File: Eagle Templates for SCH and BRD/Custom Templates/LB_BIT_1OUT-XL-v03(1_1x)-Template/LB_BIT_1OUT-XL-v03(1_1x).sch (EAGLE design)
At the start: 7 parts, among them U6 LV321SOT23-5

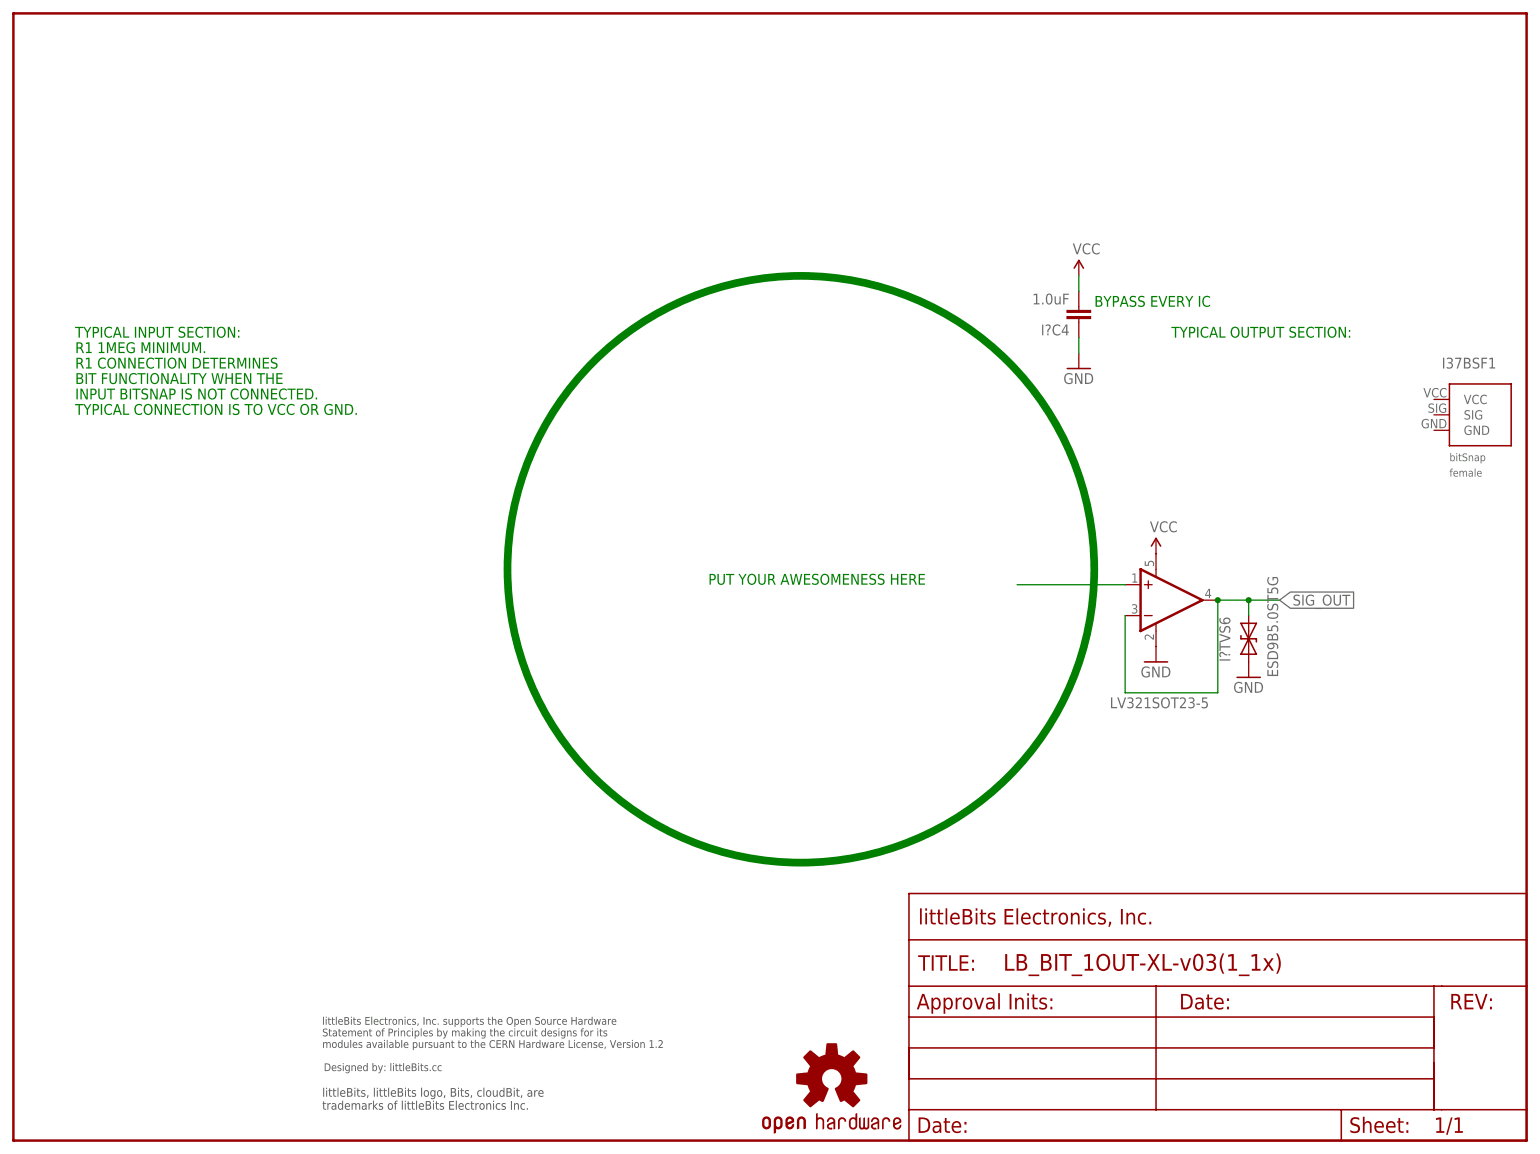
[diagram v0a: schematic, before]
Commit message: Updated templates
- Added ferrite beads
- Moved text and annotations off of Nets layer
- Minor layout changes
- Removed I/O/W prefix from reference designators
- Removed output stage components from output bits
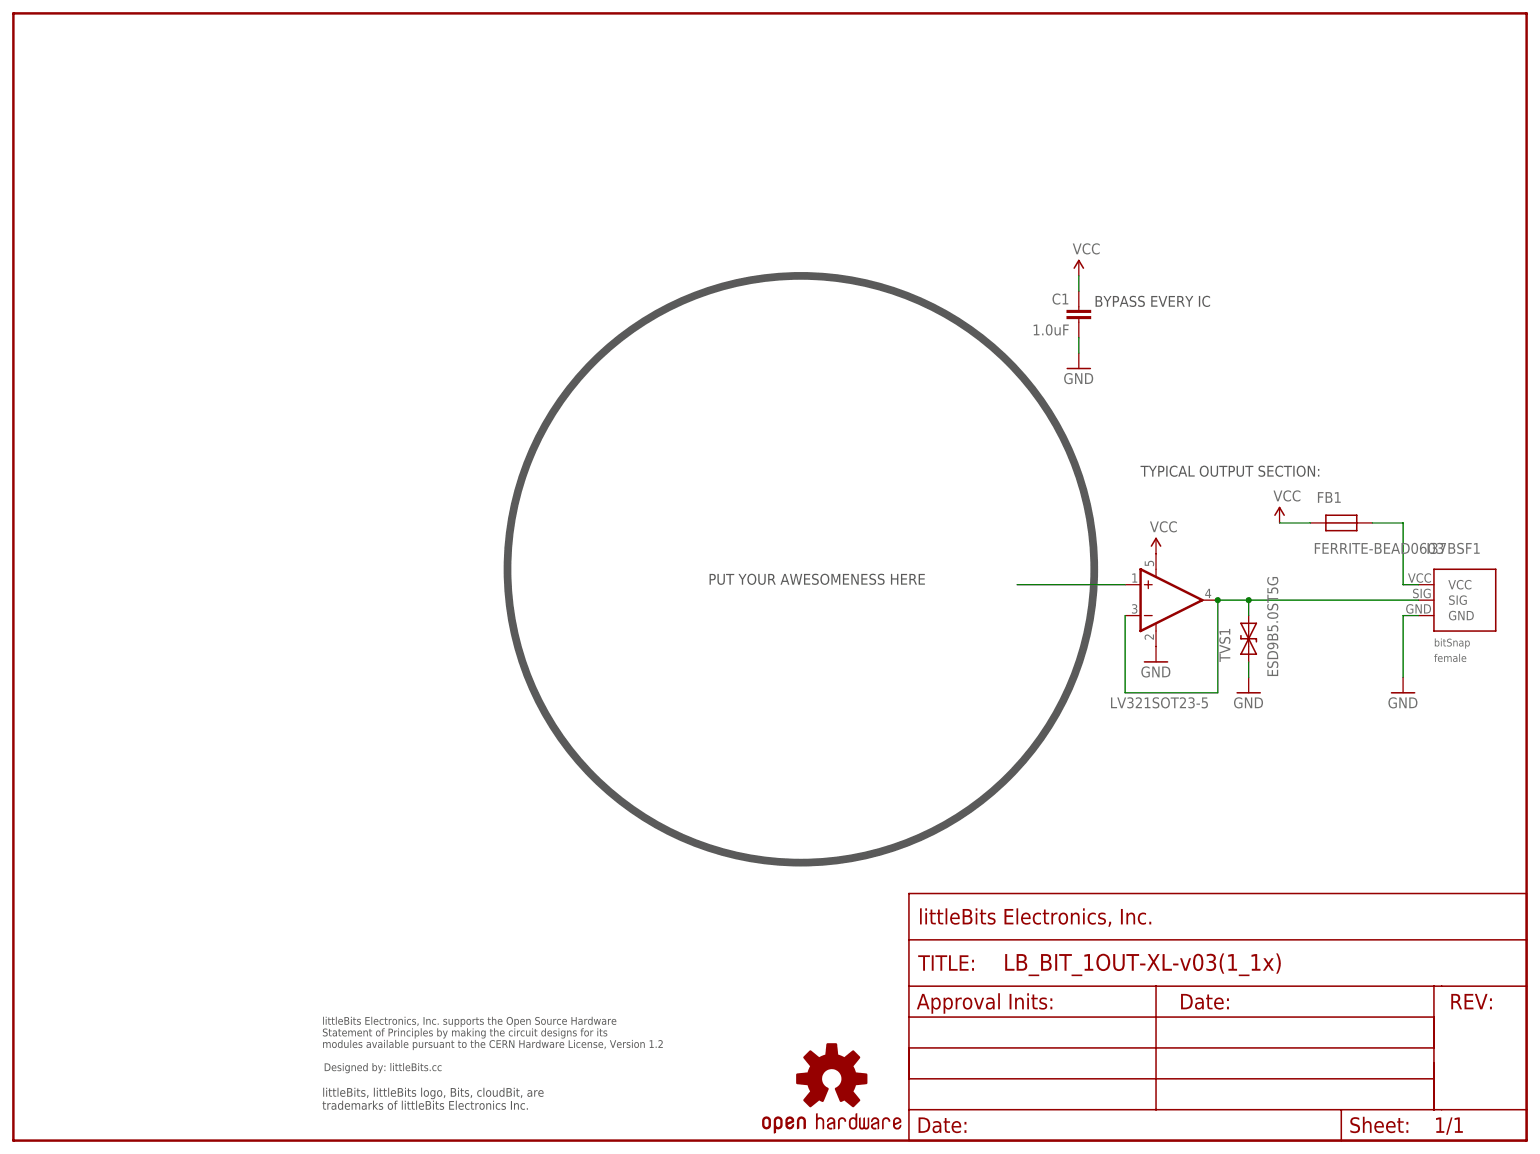
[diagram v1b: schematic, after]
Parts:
- added FB1: FERRITE-BEAD0603, LITTLEBITS:FERRITE-BEAD0603
- FRAME1: value FRAME-LETTER -> FRAME-LETTERWHITEMASK; device LITTLEBITS:FRAME-LETTER -> LITTLEBITS:FRAME-LETTERWHITEMASK
- renumbered I?C4 to C1, I?TVS6 to TVS1, U6 to U1
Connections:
- new net N$1: FB1.P$1, I37BSF1.VCC
- net GND: now also I37BSF1.GND
- net SIG_OUT: now also I37BSF1.SIG
- net VCC: now also FB1.P$2
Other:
- note removed: "BIT FUNCTIONALITY WHEN THE"
- note removed: "INPUT BITSNAP IS NOT CONNECTED."
- note removed: "R1 1MEG MINIMUM."
- note removed: "R1 CONNECTION DETERMINES"
- note removed: "TYPICAL CONNECTION IS TO VCC OR GND."
- note removed: "TYPICAL INPUT SECTION:"
- moved on the sheet: I37BSF1
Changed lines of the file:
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@@
 <?xml version="1.0" encoding="utf-8"?>
 <!DOCTYPE eagle SYSTEM "eagle.dtd">
-<eagle version="6.6.0">
+<eagle version="6.5.0">
 <drawing>
 <settings>
@@
 <layer number="56" name="wert" color="7" fill="1" visible="no" active="no"/>
 <layer number="57" name="tCAD" color="7" fill="1" visible="no" active="no"/>
+<layer number="90" name="Modules" color="5" fill="1" visible="no" active="yes"/>
 <layer number="91" name="Nets" color="2" fill="1" visible="yes" active="yes"/>
 <layer number="92" name="Busses" color="1" fill="1" visible="yes" active="yes"/>
@@
 <layer number="97" name="Info" color="7" fill="1" visible="yes" active="yes"/>
 <layer number="98" name="Guide" color="6" fill="1" visible="no" active="yes"/>
+<layer number="99" name="SpiceOrder" color="7" fill="1" visible="no" active="no"/>
 <layer number="100" name="Muster" color="7" fill="1" visible="no" active="no"/>
 <layer number="101" name="Patch_Top" color="12" fill="4" visible="no" active="yes"/>
@@
 <layer number="251" name="SMDround" color="12" fill="11" visible="no" active="no"/>
 <layer number="254" name="cooling" color="7" fill="1" visible="no" active="yes"/>
+<layer number="255" name="routoute" color="7" fill="1" visible="no" active="yes"/>
 </layers>
 <schematic>
@@
 <part name="I37BSF1" library="bitSnap" deviceset="BITSNAP_V03_FEMALE" device=""/>
 <part name="U$3" library="SparkFun" deviceset="OSHW-LOGO" device="L"/>
-<part name="I?C4" library="LITTLEBITS" deviceset="CAP" device="CAP-0603" value="1.0uF">
+<part name="C1" library="LITTLEBITS" deviceset="CAP" device="CAP-0603" value="1.0uF">
 <attribute name="COMPOSITION" value=""/>
 <attribute name="LB_PN" value=""/>
@@
 <part name="GND17" library="SparkFun" deviceset="GND" device=""/>
 <part name="P+2" library="SparkFun" deviceset="VCC" device=""/>
-<part name="U6" library="LITTLEBITS" deviceset="LV321" device="SOT23-5"/>
+<part name="U1" library="LITTLEBITS" deviceset="LV321" device="SOT23-5"/>
 <part name="GND18" library="SparkFun" deviceset="GND" device=""/>
 <part name="P+3" library="SparkFun" deviceset="VCC" device=""/>
 <part name="GND19" library="SparkFun" deviceset="GND" device=""/>
-<part name="I?TVS6" library="LITTLEBITS" deviceset="DIODE-TVS" device="SOD-923" value="ESD9B5.0ST5G"/>
+<part name="TVS1" library="LITTLEBITS" deviceset="DIODE-TVS" device="SOD-923" value="ESD9B5.0ST5G"/>
 <part name="U$1" library="LITTLEBITS" deviceset="OSHWCREDIT" device=""/>
-<part name="FRAME1" library="LITTLEBITS" deviceset="FRAME-LETTER" device=""/>
+<part name="FRAME1" library="LITTLEBITS" deviceset="FRAME-LETTER" device="WHITEMASK"/>
+<part name="FB1" library="LITTLEBITS" deviceset="FERRITE-BEAD" device="0603"/>
+<part name="P+1" library="SparkFun" deviceset="VCC" device=""/>
+<part name="GND1" library="SparkFun" deviceset="GND" device=""/>
 </parts>
 <sheets>
 <sheet>
 <plain>
-<text x="10.16" y="129.54" size="1.778" layer="91">R1 1MEG MINIMUM.</text>
-<text x="10.16" y="127" size="1.778" layer="91">R1 CONNECTION DETERMINES</text>
-<text x="10.16" y="124.46" size="1.778" layer="91">BIT FUNCTIONALITY WHEN THE</text>
-<text x="10.16" y="121.92" size="1.778" layer="91">INPUT BITSNAP IS NOT CONNECTED.</text>
-<text x="10.16" y="119.38" size="1.778" layer="91">TYPICAL CONNECTION IS TO VCC OR GND.</text>
-<text x="10.16" y="132.08" size="1.778" layer="91">TYPICAL INPUT SECTION:</text>
-<circle x="129.54" y="93.98" radius="48.26" width="1.27" layer="91"/>
-<text x="114.3" y="91.44" size="1.778" layer="91">PUT YOUR AWESOMENESS HERE</text>
-<text x="190.5" y="132.08" size="1.778" layer="91">TYPICAL OUTPUT SECTION:</text>
-<text x="177.8" y="137.16" size="1.778" layer="91">BYPASS EVERY IC</text>
+<circle x="129.54" y="93.98" radius="48.26" width="1.27" layer="97"/>
+<text x="114.3" y="91.44" size="1.778" layer="97">PUT YOUR AWESOMENESS HERE</text>
+<text x="185.42" y="109.22" size="1.778" layer="97">TYPICAL OUTPUT SECTION:</text>
+<text x="177.8" y="137.16" size="1.778" layer="97">BYPASS EVERY IC</text>
 </plain>
 <instances>
-<instance part="I37BSF1" gate="G$1" x="236.22" y="114.3"/>
+<instance part="I37BSF1" gate="G$1" x="233.68" y="83.82"/>
 <instance part="U$3" gate="G$1" x="134.62" y="10.16"/>
-<instance part="I?C4" gate="G$1" x="175.26" y="137.16" smashed="yes" rot="R180">
-<attribute name="NAME" x="173.736" y="134.239" size="1.778" layer="95" rot="R180"/>
-<attribute name="VALUE" x="173.736" y="139.319" size="1.778" layer="96" rot="R180"/>
+<instance part="C1" gate="G$1" x="175.26" y="137.16" smashed="yes" rot="R180">
+<attribute name="NAME" x="173.736" y="139.319" size="1.778" layer="95" rot="R180"/>
+<attribute name="VALUE" x="173.736" y="134.239" size="1.778" layer="96" rot="R180"/>
 </instance>
 <instance part="GND17" gate="1" x="175.26" y="127"/>
 <instance part="P+2" gate="1" x="175.26" y="142.24"/>
-<instance part="U6" gate="G$1" x="190.5" y="88.9" smashed="yes">
+<instance part="U1" gate="G$1" x="190.5" y="88.9" smashed="yes">
 <attribute name="VALUE" x="180.34" y="71.12" size="1.778" layer="96"/>
 </instance>
 <instance part="GND18" gate="1" x="187.96" y="78.74"/>
 <instance part="P+3" gate="1" x="187.96" y="96.52"/>
-<instance part="GND19" gate="1" x="203.2" y="76.2"/>
-<instance part="I?TVS6" gate="G$1" x="203.2" y="83.82" smashed="yes">
+<instance part="GND19" gate="1" x="203.2" y="73.66"/>
+<instance part="TVS1" gate="G$1" x="203.2" y="83.82" smashed="yes">
 <attribute name="NAME" x="200.1774" y="78.74" size="1.778" layer="95" rot="R90"/>
 <attribute name="VALUE" x="208.0514" y="76.2" size="1.778" layer="96" rot="R90"/>
@@
 <instance part="FRAME1" gate="G$1" x="0" y="0"/>
 <instance part="FRAME1" gate="G$2" x="147.32" y="0"/>
+<instance part="FB1" gate="G$1" x="218.44" y="101.6"/>
+<instance part="P+1" gate="1" x="208.28" y="101.6"/>
+<instance part="GND1" gate="1" x="228.6" y="73.66"/>
 </instances>
 <busses>
@@
 <segment>
 <pinref part="P+2" gate="1" pin="VCC"/>
-<pinref part="I?C4" gate="G$1" pin="2"/>
+<pinref part="C1" gate="G$1" pin="2"/>
 <wire x1="175.26" y1="142.24" x2="175.26" y2="139.7" width="0.1524" layer="91"/>
 </segment>
 <segment>
-<pinref part="U6" gate="G$1" pin="V+"/>
+<pinref part="U1" gate="G$1" pin="V+"/>
 <pinref part="P+3" gate="1" pin="VCC"/>
 </segment>
+<segment>
+<pinref part="FB1" gate="G$1" pin="P$2"/>
+<wire x1="213.36" y1="101.6" x2="208.28" y2="101.6" width="0.1524" layer="91"/>
+<pinref part="P+1" gate="1" pin="VCC"/>
+</segment>
 </net>
 <net name="GND" class="0">
 <segment>
 <pinref part="GND17" gate="1" pin="GND"/>
-<pinref part="I?C4" gate="G$1" pin="1"/>
+<pinref part="C1" gate="G$1" pin="1"/>
 <wire x1="175.26" y1="132.08" x2="175.26" y2="129.54" width="0.1524" layer="91"/>
 </segment>
 <segment>
-<pinref part="U6" gate="G$1" pin="V-"/>
+<pinref part="U1" gate="G$1" pin="V-"/>
 <pinref part="GND18" gate="1" pin="GND"/>
 </segment>
 <segment>
-<pinref part="I?TVS6" gate="G$1" pin="A"/>
+<pinref part="TVS1" gate="G$1" pin="A"/>
 <pinref part="GND19" gate="1" pin="GND"/>
+<wire x1="203.2" y1="76.2" x2="203.2" y2="78.74" width="0.1524" layer="91"/>
+</segment>
+<segment>
+<pinref part="I37BSF1" gate="G$1" pin="GND"/>
+<wire x1="231.14" y1="86.36" x2="228.6" y2="86.36" width="0.1524" layer="91"/>
+<wire x1="228.6" y1="86.36" x2="228.6" y2="76.2" width="0.1524" layer="91"/>
+<pinref part="GND1" gate="1" pin="GND"/>
 </segment>
 </net>
 <net name="SIG_OUT" class="0">
 <segment>
-<label x="208.28" y="88.9" size="1.778" layer="95" xref="yes"/>
-</segment>
-<segment>
-<pinref part="U6" gate="G$1" pin="-IN"/>
+<pinref part="U1" gate="G$1" pin="-IN"/>
 <wire x1="182.88" y1="86.36" x2="182.88" y2="73.66" width="0.1524" layer="91"/>
 <wire x1="182.88" y1="73.66" x2="198.12" y2="73.66" width="0.1524" layer="91"/>
-<pinref part="U6" gate="G$1" pin="OUT"/>
+<pinref part="U1" gate="G$1" pin="OUT"/>
 <wire x1="198.12" y1="73.66" x2="198.12" y2="88.9" width="0.1524" layer="91"/>
 <wire x1="198.12" y1="88.9" x2="203.2" y2="88.9" width="0.1524" layer="91"/>
 <junction x="198.12" y="88.9"/>
-<pinref part="I?TVS6" gate="G$1" pin="C"/>
+<pinref part="TVS1" gate="G$1" pin="C"/>
 <wire x1="203.2" y1="86.36" x2="203.2" y2="88.9" width="0.1524" layer="91"/>
-<wire x1="208.28" y1="88.9" x2="203.2" y2="88.9" width="0.1524" layer="91"/>
 <junction x="203.2" y="88.9"/>
+<pinref part="I37BSF1" gate="G$1" pin="SIG"/>
+<wire x1="203.2" y1="88.9" x2="231.14" y2="88.9" width="0.1524" layer="91"/>
 </segment>
 </net>
 <net name="N$12" class="0">
 <segment>
-<pinref part="U6" gate="G$1" pin="+IN"/>
+<pinref part="U1" gate="G$1" pin="+IN"/>
 <wire x1="182.88" y1="91.44" x2="165.1" y2="91.44" width="0.1524" layer="91"/>
 </segment>
 </net>
+<net name="N$1" class="0">
+<segment>
+<pinref part="FB1" gate="G$1" pin="P$1"/>
+<wire x1="223.52" y1="101.6" x2="228.6" y2="101.6" width="0.1524" layer="91"/>
+<wire x1="228.6" y1="101.6" x2="228.6" y2="91.44" width="0.1524" layer="91"/>
+<pinref part="I37BSF1" gate="G$1" pin="VCC"/>
+<wire x1="228.6" y1="91.44" x2="231.14" y2="91.44" width="0.1524" layer="91"/>
+</segment>
+</net>
